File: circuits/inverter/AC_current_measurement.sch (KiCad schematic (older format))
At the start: 21 parts

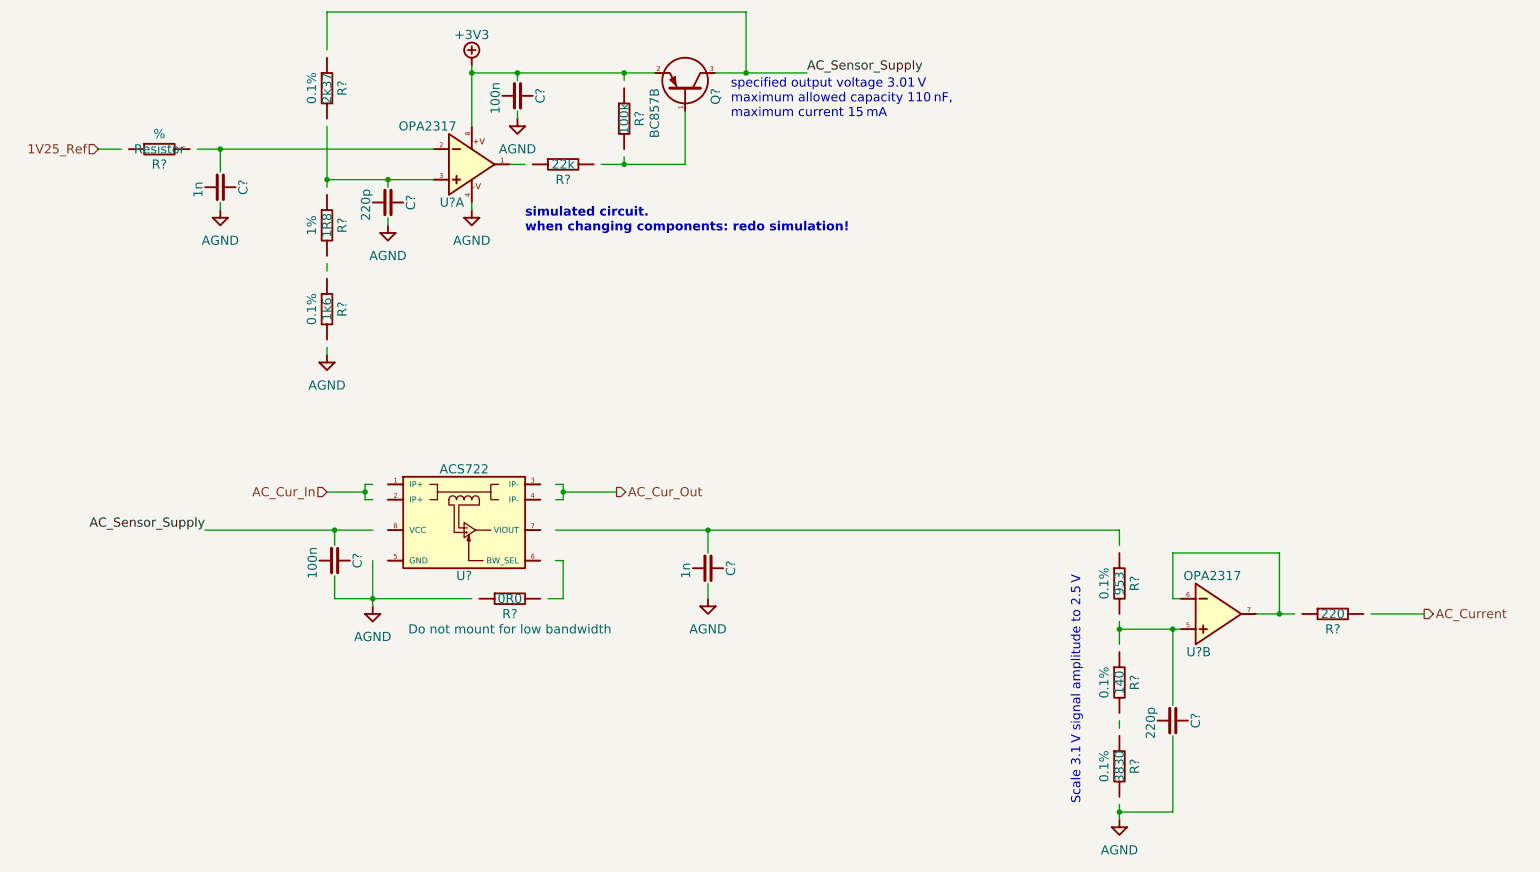
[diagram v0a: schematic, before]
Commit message: Updates all schematic pages to current components
all components are replaced with the current component library parts
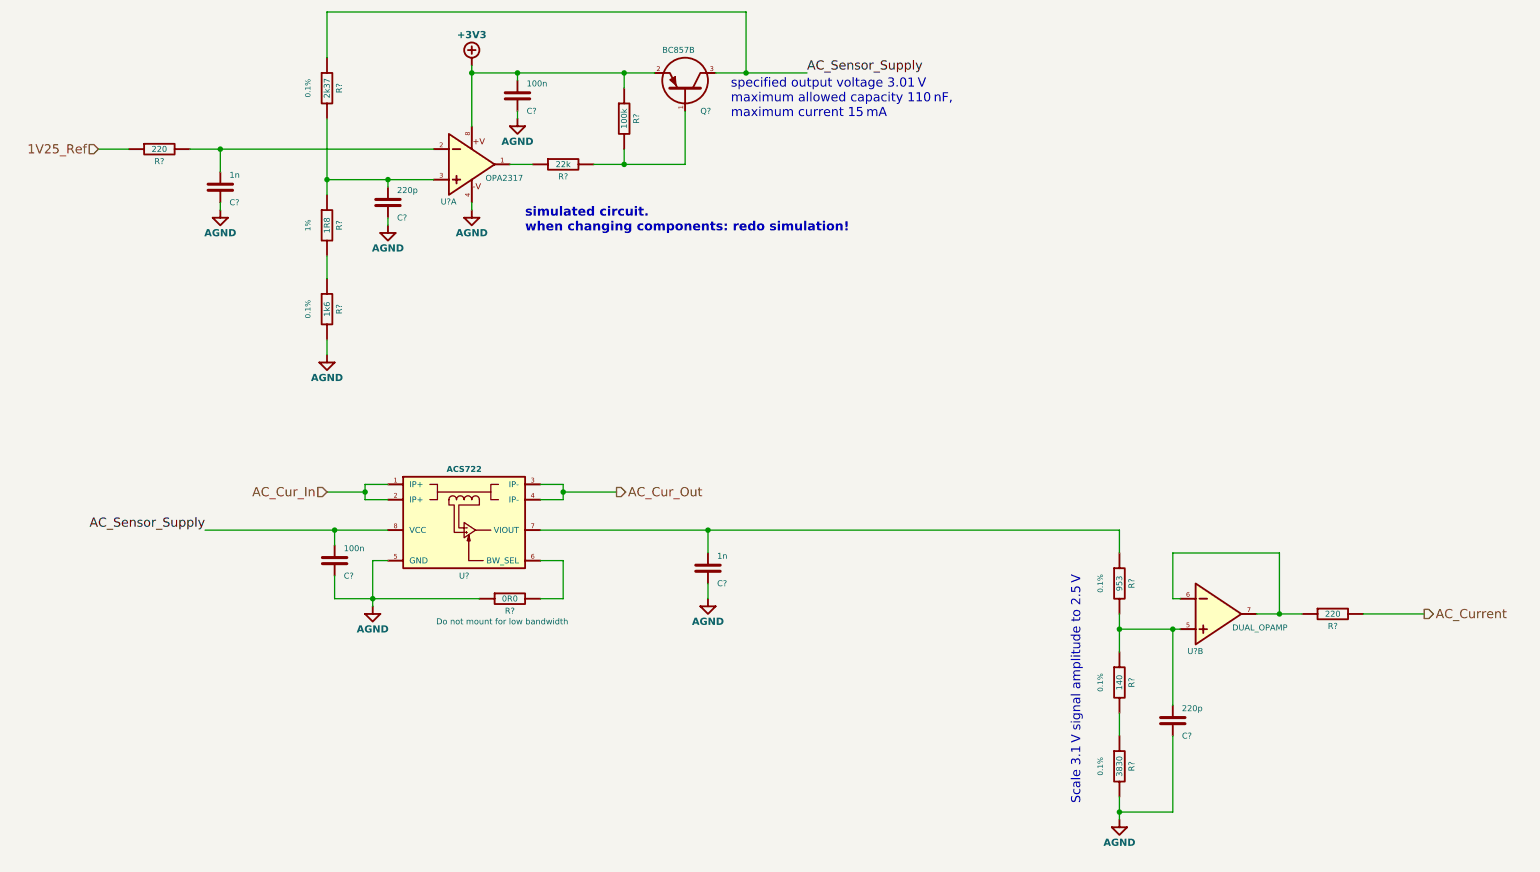
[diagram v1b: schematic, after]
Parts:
- removed C? (x2): 100n, symbol Capacitor
- removed C? (x2): 1n, symbol Capacitor
- removed C? (x2): 220p, symbol Capacitor
- removed Q?: BC857B, symbol PNP
- removed R?: 22k, symbol Resistor
- removed R?: 1R8, symbol Resistor
- removed R?: 1k6, symbol Resistor
- removed R?: 2k37, symbol Resistor
- removed R?: Resistor, symbol Resistor
- removed R?: 100k, symbol Resistor
- removed R?: 3830, symbol Resistor
- removed R?: 953, symbol Resistor
- removed R?: 220, symbol Resistor
- removed R?: 140, symbol Resistor
- removed R?: 0R0, symbol Resistor
- removed U? (x2): OPA2317, symbol DUAL_OPAMP
- removed U?: ACS722, symbol ACS722
- added C? (x2): 1n, symbol Capacitor
- added C? (x2): 220p, symbol Capacitor
- added C? (x2): 100n, symbol Capacitor
- added Q?: BC857B, symbol PNP
- added R? (x2): 220, symbol Resistor
- added R?: 2k37, symbol Resistor
- added R?: 1k6, symbol Resistor
- added R?: 1R8, symbol Resistor
- added R?: 22k, symbol Resistor
- added R?: 100k, symbol Resistor
- added R?: 0R0, symbol Resistor
- added R?: 953, symbol Resistor
- added R?: 140, symbol Resistor
- added R?: 3830, symbol Resistor
- added U?: OPA2317, symbol DUAL_OPAMP
- added U?: ACS722, symbol ACS722
- added U?: DUAL_OPAMP, symbol DUAL_OPAMP
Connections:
- wire segments 75 -> 58

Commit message: bulk-updates libraries and schematics
schematic is updated to Kicad 5.1.14
updates various sheets with new circuits
adds various component libraries
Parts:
- C? (x6): symbol Capacitor -> OSSI_standard_components:Capacitor
- Q?: symbol PNP -> OSSI_standard_components:PNP
- R? (x11): symbol Resistor -> OSSI_standard_components:Resistor
- U?: symbol DUAL_OPAMP -> OSSI_standard_components:DUAL_OPAMP
- U?: symbol ACS722 -> acs722:ACS722
- U?: value DUAL_OPAMP -> OPA2317; symbol DUAL_OPAMP -> OSSI_standard_components:DUAL_OPAMP
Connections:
- net AC_Sensor_Supply: now also Q?.C; no longer Q?.3 (C)
- net AGND: now reaches C?.1
- net AGND: now also C?.1, C?.1, C?.1, C?.1, C?.1, R?.1, R?.2, R?.2, U?.4, U?.5 (GND)
- net +3V3: now reaches C?.2, R?.1, U?.8
- net +3V3: now also Q?.E; no longer Q?.2 (E)
- net at R?.2, R?.2: now also Q?.B; no longer Q?.1 (B)
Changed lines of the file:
@@
-EESchema Schematic File Version 2
-LIBS:lm317
-LIBS:kv30f
-LIBS:OSSI_standard_components
-LIBS:connectors
-LIBS:lm4030
-LIBS:acs722
+EESchema Schematic File Version 4
 LIBS:OSSI_MK_I-cache
-EELAYER 25 0
+EELAYER 30 0
 EELAYER END
 $Descr A4 11693 8268
 encoding utf-8
-Sheet 9 11
+Sheet 7 11
 Title "AC current measurement"
 Date "2016-03-12"
@@
 1V25_Ref
 Wire Wire Line
-	3550 1100 3550 1500
+	3550 1100 3550 1150
 Wire Wire Line
 	3850 1200 3850 1150
 Wire Wire Line
-	3550 1150 4750 1150
+	3550 1150 3850 1150
 Connection ~ 3550 1150
 Wire Wire Line
@@
 	3000 2100 3000 2150
 Wire Wire Line
-	2600 1850 3300 1850
+	2600 1850 3000 1850
 Wire Wire Line
 	3000 1850 3000 1900
@@
 	2600 2350 2600 2500
 Wire Wire Line
-	2600 1450 2600 1950
+	2600 1450 2600 1850
 Connection ~ 3000 1850
 Wire Wire Line
 	1100 1650 1300 1650
 Wire Wire Line
-	1700 1650 3300 1650
+	1700 1650 1900 1650
 Wire Wire Line
 	1900 1800 1900 1650
@@
 Connection ~ 4550 1150
 Wire Wire Line
-	4350 1750 4950 1750
+	4350 1750 4550 1750
 Wire Wire Line
 	4950 1750 4950 1400
@@
 Connection ~ 4550 1750
 Wire Wire Line
-	5150 1150 5750 1150
+	5150 1150 5350 1150
 Connection ~ 5350 1150
 Text Notes 5250 1450 0    60   ~ 0
@@
 simulated circuit.\nwhen changing components: redo simulation!
 Wire Wire Line
-	7800 4800 8200 4800
-Wire Wire Line
-	7800 4700 7800 4950
+	7800 4800 8150 4800
+Wire Wire Line
+	7800 4700 7800 4800
 Connection ~ 7800 4800
 Wire Wire Line
-	7800 5900 7800 6050
-Wire Wire Line
-	8700 4700 9000 4700
+	7800 5900 7800 6000
+Wire Wire Line
+	8700 4700 8850 4700
 Wire Wire Line
 	9400 4700 9800 4700
@@
 Scale 3.1 V signal amplitude to 2.5 V
 Wire Wire Line
-	1800 4150 3000 4150
+	1800 4150 2650 4150
 Wire Wire Line
 	2650 4250 2650 4150
 Connection ~ 2650 4150
 Wire Wire Line
-	2650 4600 3600 4600
-Wire Wire Line
-	2900 4350 2900 4650
+	2650 4600 2900 4600
+Wire Wire Line
+	2900 4350 2900 4600
 Connection ~ 2900 4600
 Wire Wire Line
@@
 	2850 3850 3000 3850
 Wire Wire Line
-	2850 3850 2850 3950
+	2850 3850 2850 3900
 Wire Wire Line
 	2850 3950 3000 3950
@@
 	4000 3850 4150 3850
 Wire Wire Line
-	4150 3850 4150 3950
+	4150 3850 4150 3900
 Wire Wire Line
 	4150 3950 4000 3950
@@
 	2650 4450 2650 4600
 Wire Wire Line
-	4000 4150 7800 4150
+	4000 4150 5100 4150
 Wire Wire Line
 	7800 4150 7800 4300
@@
 Connection ~ 5100 4150
 $Comp
-L Resistor R?
+L OSSI_standard_components:Resistor R?
 U 1 1 58DD9EAE
 P 1500 1650
@@
 $EndComp
 $Comp
-L Capacitor C?
+L OSSI_standard_components:Capacitor C?
 U 1 1 58DDA0EE
 P 1900 1900
@@
 $EndComp
 $Comp
-L Resistor R?
+L OSSI_standard_components:Resistor R?
 U 1 1 58DDA6B2
 P 2600 1250
@@
 $EndComp
 $Comp
-L Resistor R?
+L OSSI_standard_components:Resistor R?
 U 1 1 58DDA916
 P 2600 2700
@@
 $EndComp
 $Comp
-L Resistor R?
+L OSSI_standard_components:Resistor R?
 U 1 1 58DDA9E0
 P 2600 2150
@@
 $EndComp
 $Comp
-L Capacitor C?
+L OSSI_standard_components:Capacitor C?
 U 1 1 58DDAC9E
 P 3000 2000
@@
 $EndComp
 $Comp
-L Capacitor C?
+L OSSI_standard_components:Capacitor C?
 U 1 1 58DDAD82
 P 3850 1300
@@
 $EndComp
 $Comp
-L Resistor R?
+L OSSI_standard_components:Resistor R?
 U 1 1 58DDAEA8
 P 4150 1750
@@
 $EndComp
 $Comp
-L Resistor R?
+L OSSI_standard_components:Resistor R?
 U 1 1 58DDB262
 P 4550 1450
@@
 $EndComp
 $Comp
-L PNP Q?
+L OSSI_standard_components:PNP Q?
 U 1 1 58DDB2F2
 P 4950 1250
@@
 $EndComp
 $Comp
-L DUAL_OPAMP U?
+L OSSI_standard_components:DUAL_OPAMP U?
 U 1 1 58DDB6E0
 P 3500 1750
@@
 $EndComp
 $Comp
-L AGND #AGND?
+L OSSI_standard_components:AGND #AGND?
 U 1 1 58DDB8D1
 P 3850 1450
@@
 $EndComp
 $Comp
-L AGND #AGND?
+L OSSI_standard_components:AGND #AGND?
 U 1 1 58DDB9D9
 P 3550 2050
@@
 $EndComp
 $Comp
-L AGND #AGND?
+L OSSI_standard_components:AGND #AGND?
 U 1 1 58DDBA23
 P 3000 2150
@@
 $EndComp
 $Comp
-L AGND #AGND?
+L OSSI_standard_components:AGND #AGND?
 U 1 1 58DDBA6D
 P 2600 3000
@@
 $EndComp
 $Comp
-L AGND #AGND?
+L OSSI_standard_components:AGND #AGND?
 U 1 1 58DDBAB7
 P 1900 2050
@@
 $EndComp
 $Comp
-L ACS722 U?
+L acs722:ACS722 U?
 U 1 1 58DDCB30
 P 3500 4100
@@
 	2900 4350 3000 4350
 $Comp
-L Capacitor C?
+L OSSI_standard_components:Capacitor C?
 U 1 1 58DDD126
 P 2650 4350
@@
 $EndComp
 $Comp
-L Resistor R?
+L OSSI_standard_components:Resistor R?
 U 1 1 58DDD4C7
 P 3800 4600
@@
 $EndComp
 $Comp
-L Capacitor C?
+L OSSI_standard_components:Capacitor C?
 U 1 1 58DDE168
 P 5100 4400
@@
 $EndComp
 $Comp
-L DUAL_OPAMP U?
+L OSSI_standard_components:DUAL_OPAMP U?
 U 2 1 58DDE44A
 P 8400 4700
 F 0 "U?" H 8350 4455 39  0000 R CNN
-F 1 "DUAL_OPAMP" H 8540 4610 39  0000 L CNN
+F 1 "OPA2317" H 8540 4610 39  0000 L CNN
 F 2 "" H 8350 4700 60  0000 C CNN
 F 3 "" H 8350 4700 60  0000 C CNN
@@
 $EndComp
 $Comp
-L Resistor R?
+L OSSI_standard_components:Resistor R?
 U 1 1 58DDE9CA
 P 9200 4700
@@
 $EndComp
 $Comp
-L Capacitor C?
+L OSSI_standard_components:Capacitor C?
 U 1 1 58DDEED6
 P 8150 5400
@@
 $EndComp
 $Comp
-L Resistor R?
+L OSSI_standard_components:Resistor R?
 U 1 1 58DDF03F
 P 7800 4500
@@
 $EndComp
 $Comp
-L Resistor R?
+L OSSI_standard_components:Resistor R?
 U 1 1 58DDF2EB
 P 7800 5150
@@
 $EndComp
 $Comp
-L Resistor R?
+L OSSI_standard_components:Resistor R?
 U 1 1 58DDF389
 P 7800 5700
@@
 $EndComp
 $Comp
-L +3V3 #+3V3?
+L OSSI_standard_components:+3V3 #+3V3?
 U 1 1 58DE0718
 P 3550 1100
@@
 $EndComp
 $Comp
-L AGND #AGND?
+L OSSI_standard_components:AGND #AGND?
 U 1 1 58E34939
 P 2900 4650
@@
 $EndComp
 $Comp
-L AGND #AGND?
+L OSSI_standard_components:AGND #AGND?
 U 1 1 58E34983
 P 5100 4600
@@
 $EndComp
 $Comp
-L AGND #AGND?
+L OSSI_standard_components:AGND #AGND?
 U 1 1 58E349CD
 P 7800 6050
@@
 	1    0    0    -1
 $EndComp
+Wire Wire Line
+	3550 1150 3550 1500
+Wire Wire Line
+	3000 1850 3300 1850
+Wire Wire Line
+	1900 1650 3300 1650
+Wire Wire Line
+	2600 1850 2600 1950
+Wire Wire Line
+	3850 1150 4550 1150
+Wire Wire Line
+	4550 1150 4750 1150
+Wire Wire Line
+	4550 1750 4950 1750
+Wire Wire Line
+	5350 1150 5750 1150
+Wire Wire Line
+	7800 4800 7800 4950
+Wire Wire Line
+	8850 4700 9000 4700
+Wire Wire Line
+	8150 4800 8200 4800
+Wire Wire Line
+	7800 6000 7800 6050
+Wire Wire Line
+	2650 4150 3000 4150
+Wire Wire Line
+	2900 4600 3600 4600
+Wire Wire Line
+	2900 4600 2900 4650
+Wire Wire Line
+	2850 3900 2850 3950
+Wire Wire Line
+	4150 3900 4150 3950
+Wire Wire Line
+	5100 4150 7800 4150
 $EndSCHEMATC

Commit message: minor updates and cleaup
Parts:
- Q?: footprint (none) -> OSSI_standard_footprints:SOT23_BEC_R
- U? (x2): footprint (none) -> OSSI_standard_footprints:SOIC8
- U?: footprint (none) -> OSSI_standard_footprints:SOIC8_CurrentSensor
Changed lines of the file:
@@
 EESchema Schematic File Version 4
-LIBS:OSSI_MK_I-cache
 EELAYER 30 0
 EELAYER END
 $Descr A4 11693 8268
 encoding utf-8
-Sheet 7 11
+Sheet 5 12
 Title "AC current measurement"
 Date "2016-03-12"
@@
 F 0 "Q?" V 4800 1150 39  0000 R CNN
 F 1 "BC857B" V 5200 1400 39  0000 R CNN
-F 2 "" H 4850 950 60  0000 C CNN
+F 2 "OSSI_standard_footprints:SOT23_BEC_R" H 4850 950 60  0001 C CNN
 F 3 "" H 4950 1050 60  0000 C CNN
 F 4 "M" H 5150 1375 35  0001 L CNN "Manufacturer"
@@
 F 0 "U?" H 3450 1505 39  0000 R CNN
 F 1 "OPA2317" H 3640 1660 39  0000 L CNN
-F 2 "" H 3450 1750 60  0000 C CNN
+F 2 "OSSI_standard_footprints:SOIC8" H 3450 1750 60  0001 C CNN
 F 3 "" H 3450 1750 60  0000 C CNN
 F 4 "M" H 3675 1910 35  0001 L CNN "Manufacturer"
@@
 $EndComp
 $Comp
-L OSSI_standard_components:AGND #AGND?
+L OSSI_standard_components:AGND #AGND0116
 U 1 1 58DDB8D1
 P 3850 1450
-F 0 "#AGND?" H 3850 1250 39  0001 C CNN
+F 0 "#AGND0116" H 3850 1250 39  0001 C CNN
 F 1 "AGND" H 3850 1300 47  0000 C CNB
 F 2 "" H 3850 1450 60  0000 C CNN
@@
 $EndComp
 $Comp
-L OSSI_standard_components:AGND #AGND?
+L OSSI_standard_components:AGND #AGND0117
 U 1 1 58DDB9D9
 P 3550 2050
-F 0 "#AGND?" H 3550 1850 39  0001 C CNN
+F 0 "#AGND0117" H 3550 1850 39  0001 C CNN
 F 1 "AGND" H 3550 1900 47  0000 C CNB
 F 2 "" H 3550 2050 60  0000 C CNN
@@
 $EndComp
 $Comp
-L OSSI_standard_components:AGND #AGND?
+L OSSI_standard_components:AGND #AGND0118
 U 1 1 58DDBA23
 P 3000 2150
-F 0 "#AGND?" H 3000 1950 39  0001 C CNN
+F 0 "#AGND0118" H 3000 1950 39  0001 C CNN
 F 1 "AGND" H 3000 2000 47  0000 C CNB
 F 2 "" H 3000 2150 60  0000 C CNN
@@
 $EndComp
 $Comp
-L OSSI_standard_components:AGND #AGND?
+L OSSI_standard_components:AGND #AGND0119
 U 1 1 58DDBA6D
 P 2600 3000
-F 0 "#AGND?" H 2600 2800 39  0001 C CNN
+F 0 "#AGND0119" H 2600 2800 39  0001 C CNN
 F 1 "AGND" H 2600 2850 47  0000 C CNB
 F 2 "" H 2600 3000 60  0000 C CNN
@@
 $EndComp
 $Comp
-L OSSI_standard_components:AGND #AGND?
+L OSSI_standard_components:AGND #AGND0120
 U 1 1 58DDBAB7
 P 1900 2050
-F 0 "#AGND?" H 1900 1850 39  0001 C CNN
+F 0 "#AGND0120" H 1900 1850 39  0001 C CNN
 F 1 "AGND" H 1900 1900 47  0000 C CNB
 F 2 "" H 1900 2050 60  0000 C CNN
@@
 F 0 "U?" H 3500 3750 39  0000 C CNN
 F 1 "ACS722" H 3500 4450 39  0000 C CNB
-F 2 "" H 3500 4525 39  0000 C CNN
+F 2 "OSSI_standard_footprints:SOIC8_CurrentSensor" H 3500 4525 39  0001 C CNN
 F 3 "" H 3500 4150 60  0000 C CNN
 F 4 "M" H 3825 4475 35  0001 L CNN "Manufacturer"
@@
 F 0 "U?" H 8350 4455 39  0000 R CNN
 F 1 "OPA2317" H 8540 4610 39  0000 L CNN
-F 2 "" H 8350 4700 60  0000 C CNN
+F 2 "OSSI_standard_footprints:SOIC8" H 8350 4700 60  0001 C CNN
 F 3 "" H 8350 4700 60  0000 C CNN
 F 4 "M" H 8575 4860 35  0001 L CNN "Manufacturer"
@@
 $EndComp
 $Comp
-L OSSI_standard_components:+3V3 #+3V3?
+L OSSI_standard_components:+3V3 #+3V30101
 U 1 1 58DE0718
 P 3550 1100
-F 0 "#+3V3?" H 3550 1375 60  0001 C CNN
+F 0 "#+3V30101" H 3550 1375 60  0001 C CNN
 F 1 "+3V3" H 3550 1300 47  0000 C CNB
 F 2 "" H 3550 1100 60  0000 C CNN
@@
 $EndComp
 $Comp
-L OSSI_standard_components:AGND #AGND?
+L OSSI_standard_components:AGND #AGND0121
 U 1 1 58E34939
 P 2900 4650
-F 0 "#AGND?" H 2900 4450 39  0001 C CNN
+F 0 "#AGND0121" H 2900 4450 39  0001 C CNN
 F 1 "AGND" H 2900 4500 47  0000 C CNB
 F 2 "" H 2900 4650 60  0000 C CNN
@@
 $EndComp
 $Comp
-L OSSI_standard_components:AGND #AGND?
+L OSSI_standard_components:AGND #AGND0122
 U 1 1 58E34983
 P 5100 4600
-F 0 "#AGND?" H 5100 4400 39  0001 C CNN
+F 0 "#AGND0122" H 5100 4400 39  0001 C CNN
 F 1 "AGND" H 5100 4450 47  0000 C CNB
 F 2 "" H 5100 4600 60  0000 C CNN
@@
 $EndComp
 $Comp
-L OSSI_standard_components:AGND #AGND?
+L OSSI_standard_components:AGND #AGND0123
 U 1 1 58E349CD
 P 7800 6050
-F 0 "#AGND?" H 7800 5850 39  0001 C CNN
+F 0 "#AGND0123" H 7800 5850 39  0001 C CNN
 F 1 "AGND" H 7800 5900 47  0000 C CNB
 F 2 "" H 7800 6050 60  0000 C CNN
